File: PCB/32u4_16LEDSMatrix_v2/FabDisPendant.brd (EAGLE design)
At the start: 71.1 x 54.2 mm, 55 parts, among them IC1 MPR121, U1 ATMEGA32U4-AU, Y1 16MHz

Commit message: Finished PCB v2 basics
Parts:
- moved R10 17.1 mm to (44.1, 26.8), turned to 270 degrees
- moved R2 1.44 mm to (54.4, 42.2), turned to 180 degrees
- moved C20 1.27 mm to (32.1, 32.9), turned to 90 degrees
- moved S1 0.25 mm to (53.3, 48.5)
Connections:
- removed net D13: U1.32
- removed net D5: U1.31
- new net D10: U1.30
- new net D9: U1.29
- net LEDS_CI: now also U1.32; no longer U1.29
- net LEDS_DI: now also U1.31; no longer U1.30
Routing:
- net MOSI: track 0.00 -> 43.9 mm, vias 0 -> 2
- net SCK: track 27.3 -> 56.4 mm, vias 1 -> 2
- net .: track 0.00 -> 25.6 mm, vias 0 -> 1
- net RESET: track 1.93 -> 21.2 mm
- net MISO: track 0.00 -> 14.7 mm
- net LEDS_CI: track 17.4 -> 12.8 mm
- net 5V: track 142.0 -> 139.1 mm
- net RMFIRQ: track 20.7 -> 22.6 mm
- net GND: track 5.27 -> 7.11 mm, vias 3 -> 5
- net N$38: track 0.00 -> 1.54 mm
- net LEDS_DI: track 13.9 -> 13.0 mm

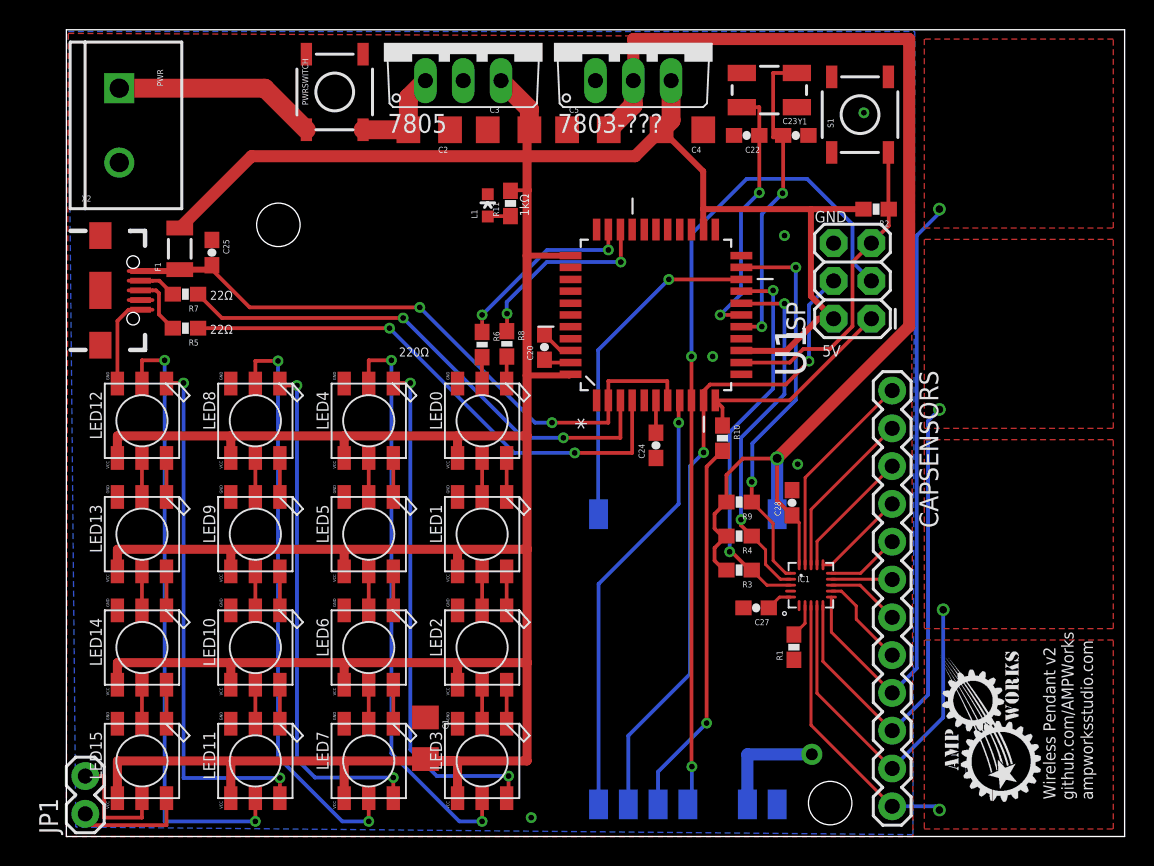
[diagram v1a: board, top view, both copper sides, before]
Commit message: Added headers for some digital and analog pins
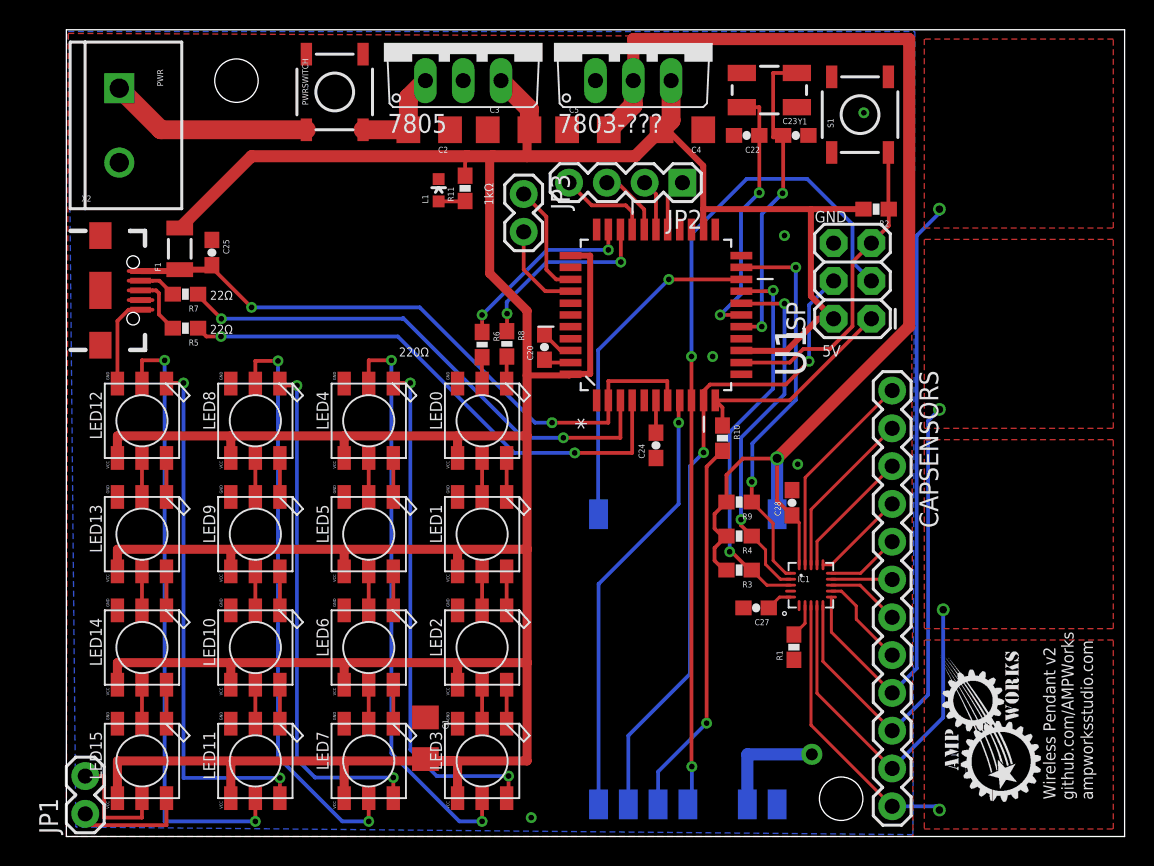
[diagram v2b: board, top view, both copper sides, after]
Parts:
- added JP2: (no value), SparkFun-Connectors:1X04
- added JP3: (no value), SparkFun-Connectors:1X02
- moved L1 3.45 mm to (25.0, 43.4)
- moved R11 3.21 mm to (26.8, 43.6)
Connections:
- net A0: now also JP3.1
- net A1: now also JP3.2
- net D10: now also JP2.4
- net D6: now also JP2.1
- net D8: now also JP2.2
- net D9: now also JP2.3
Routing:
- net 5V: track 139.1 -> 148.4 mm
- net A0: track 0.00 -> 7.61 mm
- net A1: track 0.00 -> 6.29 mm
- net D10: track 0.00 -> 6.25 mm
- net D9: track 0.00 -> 4.61 mm
- net D6: track 0.00 -> 3.56 mm
- net D8: track 0.00 -> 3.47 mm

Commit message: FInished up changes to the board
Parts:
- removed PWRSWITCH: Reset, SparkFun:TACTILE_SWITCH_SMD
- added D2: (no value), SparkFun:SOD-323
- added R12: 10k, SparkFun:0603-RES
- added SWITCH: SWITCH, SparkFun-Connectors:2X3
- R10: value 10K -> 4.7k
- moved C20 1.58 mm to (32.2, 34.5), turned to 270 degrees
- moved C4 0.46 mm to (41.7, 47.9)
- moved C5 0.36 mm to (35.1, 47.9)
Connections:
- removed net D10: JP2.4, U1.30
- removed net D9: JP2.3, U1.29
- new net D13: JP2.4, U1.32
- new net D5: JP2.3, U1.31
- new net N$37: 7803-???.3, C4.2, D2.1
- net 3.3V: now also R12.2
- net 5V: now also D2.2; no longer 7803-???.3, C4.2
- net LEDS_CI: now also U1.30; no longer U1.32
- net LEDS_DI: now also U1.29; no longer U1.31
- net N$36: now also SWITCH.6; no longer PWRSWITCH.1
- net RAW: now also SWITCH.4; no longer PWRSWITCH.3
- net SS: now also R12.1
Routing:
- net RAW: track 6.82 -> 13.1 mm
- net D10: track 6.25 -> 0.00 mm
- net N$37: track 0.00 -> 5.49 mm
- net 5V: track 148.4 -> 143.4 mm
- net D9: track 4.61 -> 0.00 mm
- net D13: track 0.00 -> 4.54 mm
- net 3.3V: track 80.5 -> 84.6 mm
- net D5: track 0.00 -> 3.53 mm
- net N$36: track 13.7 -> 10.9 mm
- net LEDS_DI: track 13.0 -> 14.8 mm
- net LEDS_CI: track 12.8 -> 14.7 mm
- net GND: track 7.11 -> 6.67 mm, vias 5 -> 7
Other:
- board text added: "4.7kΩ*"
